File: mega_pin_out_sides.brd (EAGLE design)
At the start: 101.8 x 85 mm, 31 parts, among them T1 2N2222, T2 2N2222, T3 2N2222, T4 2N2222

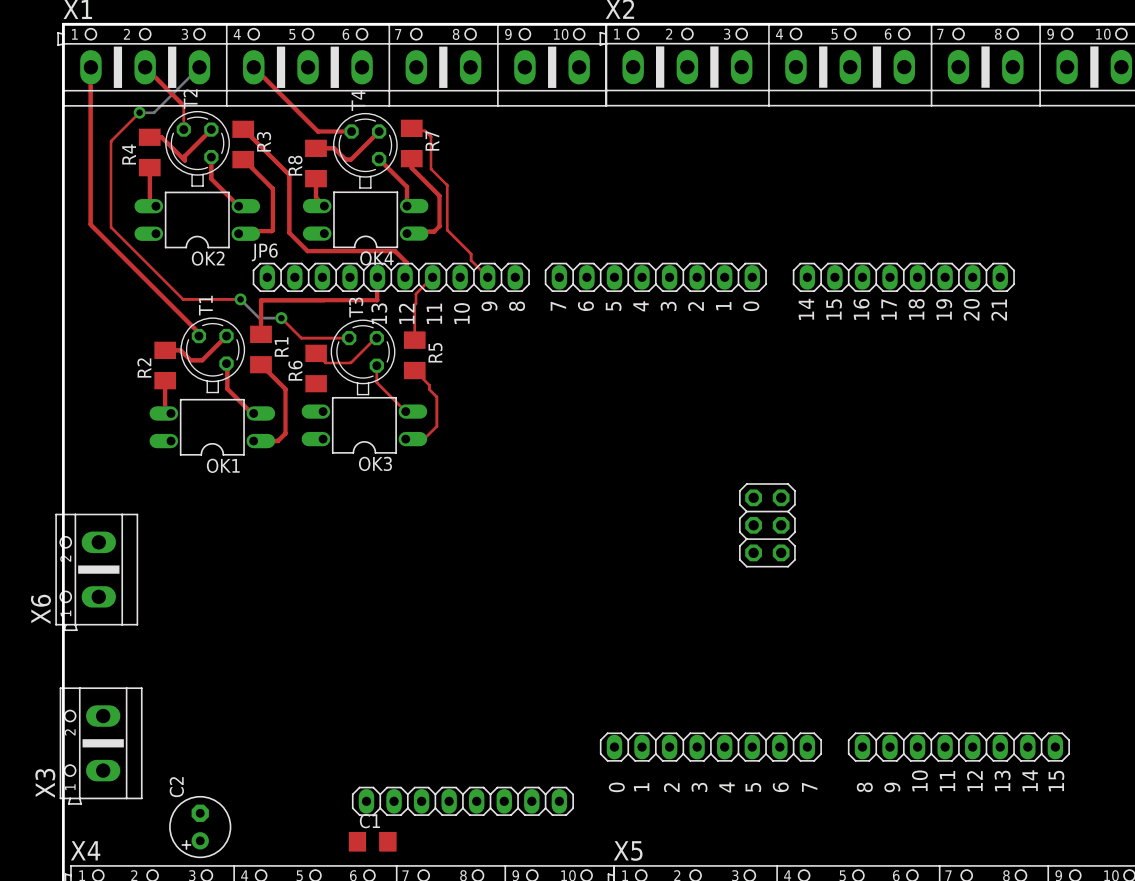
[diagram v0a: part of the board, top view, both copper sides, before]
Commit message: [SIDES] Group same components together
- Grouped same components together and till now this looks a better design solution. to be continued.
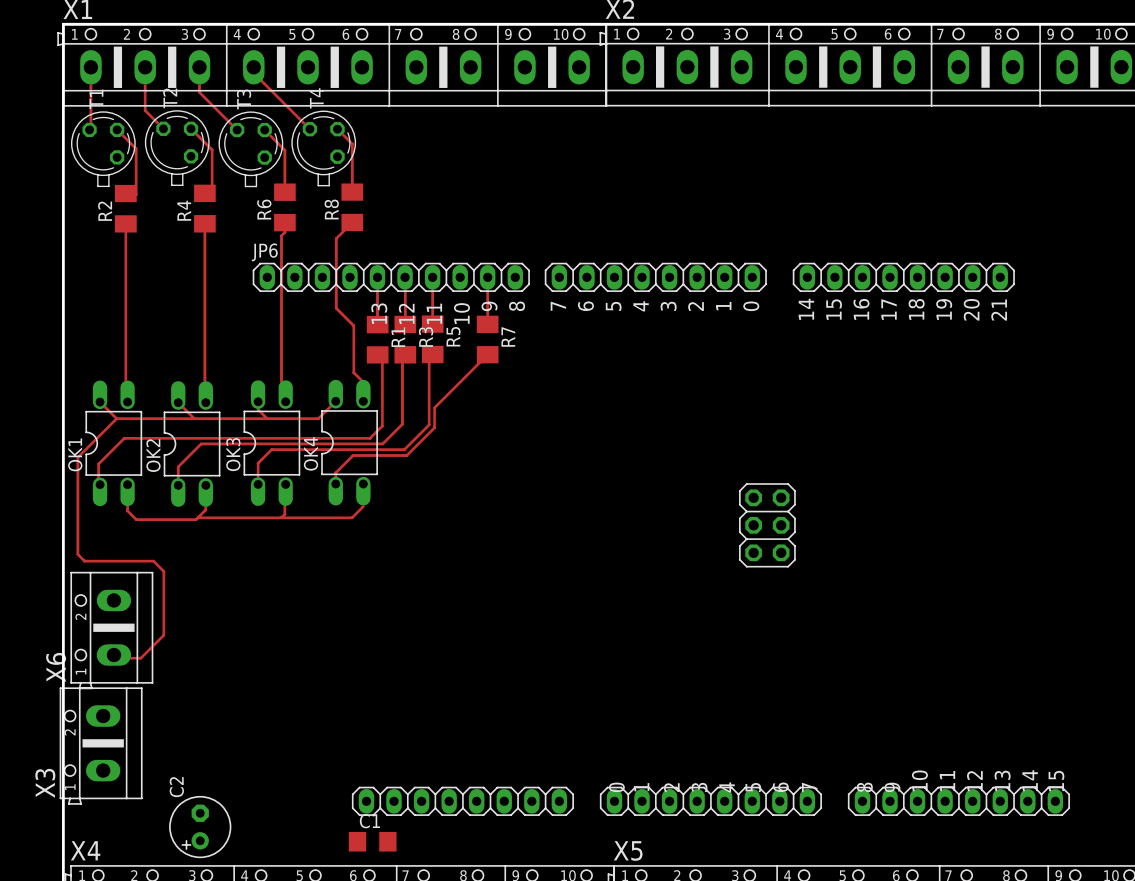
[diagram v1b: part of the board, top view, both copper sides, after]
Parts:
- moved R3 23.4 mm to (31.5, 55.9)
- moved T3 21.8 mm to (17.3, 74.0)
- moved T1 21.5 mm to (3.69, 74.0)
- moved OK2 20.7 mm to (11.9, 46.3), turned to 0 degrees
- moved OK4 20.6 mm to (26.4, 46.4), turned to 0 degrees
- moved R7 19.4 mm to (39.1, 55.9)
- moved R6 15.1 mm to (20.4, 68.1)
- moved R2 14.9 mm to (5.76, 68.0)
- moved R1 10.8 mm to (29.0, 55.9)
- moved OK1 9.20 mm to (4.65, 46.4), turned to 0 degrees
- moved OK3 8.68 mm to (19.2, 46.4), turned to 0 degrees
- moved R4 7.26 mm to (13.0, 68.0)
- moved X6 5.54 mm to (4.66, 29.4)
- moved R8 5.25 mm to (26.6, 68.1)
- moved ADCH 5.00 mm to (82.5, 13.4)
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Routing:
- net VEXT: track 0.00 -> 62.1 mm
- net 11BJT: track 45.1 -> 7.22 mm, vias 3 -> 0
- net N$1: track 10.5 -> 37.9 mm
- net 13BJT: track 28.9 -> 5.89 mm
- net 12: track 24.7 -> 4.35 mm
- net N$5: track 11.1 -> 30.5 mm
- net N$17: track 0.00 -> 16.8 mm
- net N$8: track 9.35 -> 25.8 mm
- net N$20: track 2.84 -> 18.1 mm
- net N$2: track 3.25 -> 16.5 mm
- net 9: track 17.2 -> 4.34 mm
- net N$6: track 3.80 -> 16.5 mm
- net 13: track 16.0 -> 4.36 mm
- net GND: track 22.0 -> 33.6 mm
- net N$19: track 10.6 -> 20.6 mm
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
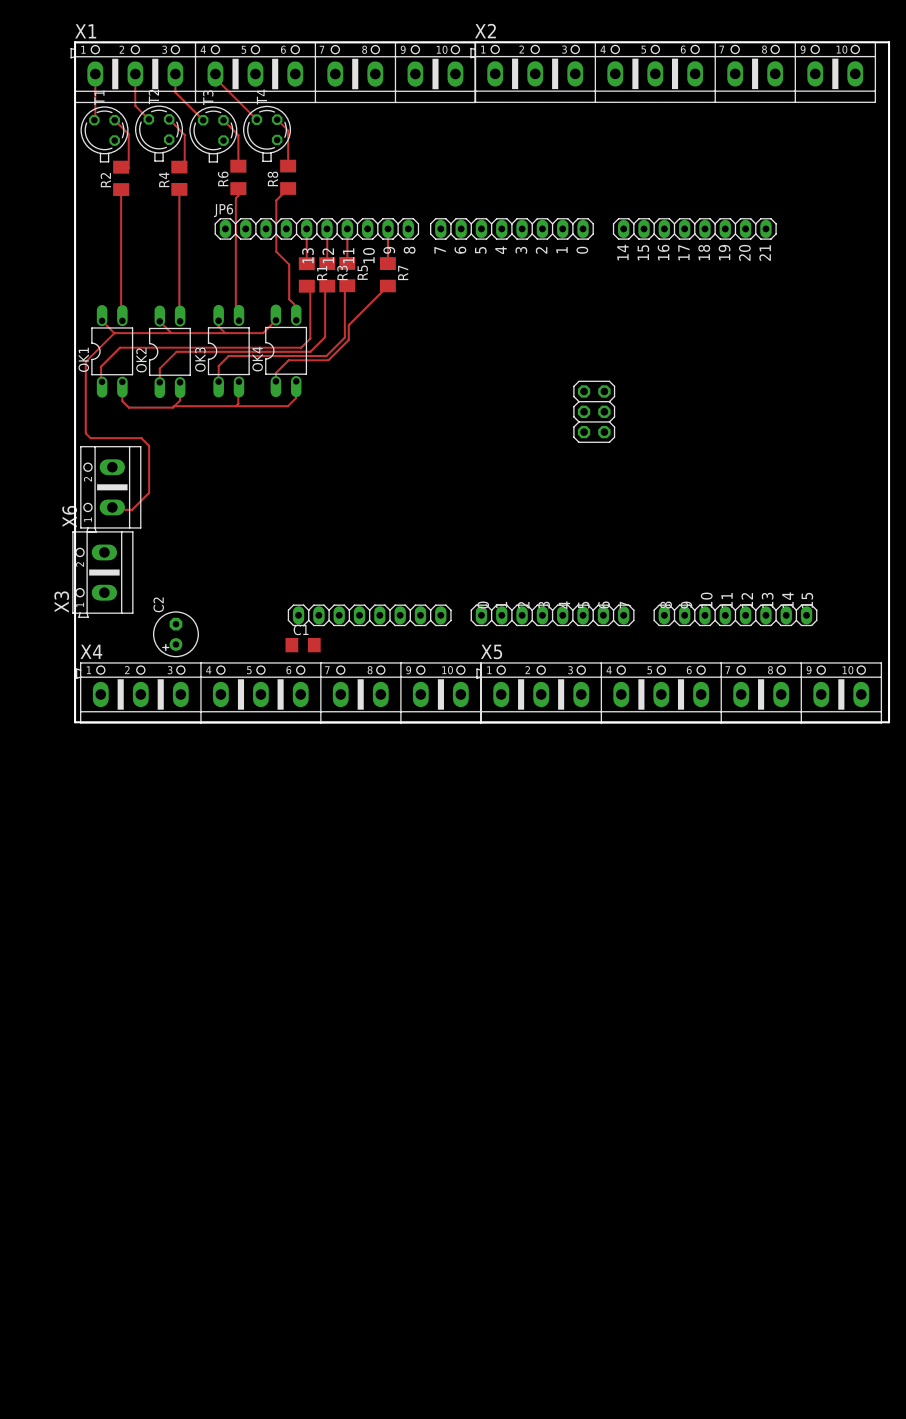
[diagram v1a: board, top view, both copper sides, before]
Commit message: Continue side Schematic design and layout
Almost finished first trail for board layout.
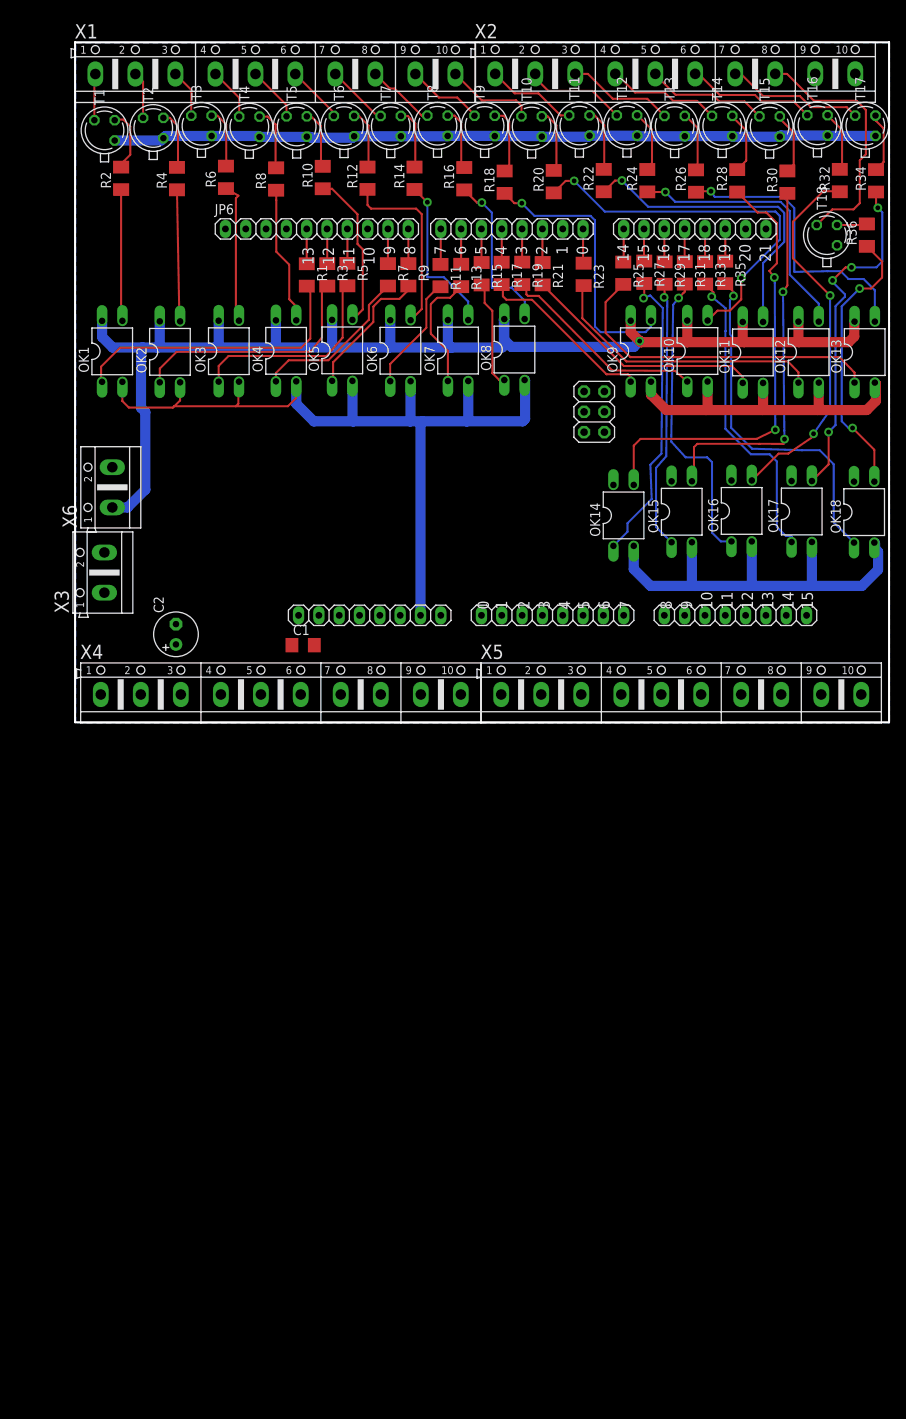
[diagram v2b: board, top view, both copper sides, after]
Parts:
- added OK10, OK11, OK12, OK13, OK14, OK15, OK16, OK17, OK18, OK5, OK6, OK7, OK8, OK9: PC817, optocoupler:DIL04
- added R10, R11, R12, R13, R14, R15, R16, R17, R18, R19, R20, R21, R22, R23, R24, R25, R26, R27, R28, R29, R30, R31, R32, R33, R34, R35, R36, R9: (no value), resistor:M1206
- added T10, T11, T12, T13, T14, T15, T16, T17, T18, T5, T6, T7, T8, T9: 2N2222, transistor:TO18
- moved T4 2.24 mm to (21.8, 74.4)
- moved T3 1.60 mm to (15.8, 74.6)
- moved R6 1.56 mm to (18.9, 68.1)
- moved R8 1.52 mm to (25.1, 67.9)
- moved T2 0.75 mm to (9.77, 74.3)
- moved R4 0.31 mm to (12.7, 68.0)
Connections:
- removed net N$16: X1.5
- new net 0: PWML.1, R23.1
- new net 0BJT: T12.3, X2.2
- new net 14: COMMUNICATION.8, R25.1
- new net 14BJT: T13.3, X2.3
- new net 15: COMMUNICATION.7, R27.1
- new net 15BJT: T14.3, X2.4
- new net 16: COMMUNICATION.6, R29.1
- new net 16BJT: T15.3, X2.5
- new net 17: COMMUNICATION.5, R31.1
- new net 17BJT: T16.3, X2.6
- new net 18: COMMUNICATION.4, R33.1
- new net 18BJT: T17.3, X2.7
- new net 19: COMMUNICATION.3, R35.1
- new net 19BJT: T18.3, X2.8
- new net 2: PWML.3, R21.1
- new net 2BJT: T11.3, X2.1
- new net 3: PWML.4, R19.1
- new net 3BJT: T10.3, X1.10
- new net 4: PWML.5, R17.1
- new net 4BJT: T9.3, X1.9
- new net 5: PWML.6, R15.1
- new net 5BJT: T8.3, X1.8
- new net 6: PWML.7, R13.1
- new net 6BJT: T7.3, X1.7
- new net 7: PWML.8, R11.1
- new net 7BJT: T6.3, X1.6
- new net 8: JP6.10, R9.1
- new net 8BJT: T5.3, X1.5
- new net N$14: OK5.1, R9.2
- new net N$15: OK5.3, R10.1
- new net N$22: R10.2, T5.2
- new net N$23: OK6.1, R11.2
- new net N$24: OK6.3, R12.1
- new net N$25: R12.2, T6.2
- new net N$26: OK7.1, R13.2
- new net N$27: OK7.3, R14.1
- new net N$28: R14.2, T7.2
- new net N$29: OK8.1, R15.2
- new net N$30: OK8.3, R16.1
- new net N$31: R16.2, T8.2
- new net N$32: OK9.1, R17.2
- new net N$33: OK9.3, R18.1
- new net N$34: R18.2, T9.2
- new net N$35: OK10.1, R19.2
- new net N$36: OK10.3, R20.1
- new net N$37: R20.2, T10.2
- new net N$38: OK11.1, R21.2
- new net N$39: OK11.3, R22.1
- new net N$40: R22.2, T11.2
- new net N$41: OK16.1, R31.2
- new net N$42: OK16.3, R32.1
- new net N$43: R32.2, T16.2
- new net N$44: OK12.1, R23.2
- new net N$45: OK12.3, R24.1
- new net N$46: R24.2, T12.2
- new net N$47: OK13.1, R25.2
- new net N$48: OK13.3, R26.1
- new net N$49: R26.2, T13.2
- new net N$50: OK14.1, R27.2
- new net N$51: OK14.3, R28.1
- new net N$52: R28.2, T14.2
- new net N$53: OK15.1, R29.2
- new net N$54: OK15.3, R30.1
- new net N$55: R30.2, T15.2
- new net N$56: OK18.1, R35.2
- new net N$57: OK18.3, R36.1
- new net N$58: R36.2, T18.2
- new net N$59: OK17.1, R33.2
- new net N$60: OK17.3, R34.1
- new net N$61: R34.2, T17.2
- new net N$77: COMMUNICATION.2
- new net N$78: COMMUNICATION.1
- new net N$92: X2.9
- new net N$93: X2.10
- net GND: now also OK10.2, OK11.2, OK12.2, OK13.2, OK14.2, OK15.2, OK16.2, OK17.2, OK18.2, OK5.2, OK6.2, OK7.2, OK8.2, OK9.2, T10.1, T11.1, T12.1, T13.1, T14.1, T15.1, T16.1, T17.1, T18.1, T5.1, T6.1, T7.1, T8.1, T9.1
- net VEXT: now also OK10.4, OK11.4, OK12.4, OK13.4, OK14.4, OK15.4, OK16.4, OK17.4, OK18.4, OK5.4, OK6.4, OK7.4, OK8.4, OK9.4
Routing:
- net GND: track 33.6 -> 305.7 mm
- net VEXT: track 62.1 -> 161.2 mm, vias 0 -> 1
- net N$51: track 0.00 -> 56.2 mm, vias 0 -> 2
- net N$36: track 0.00 -> 48.4 mm, vias 0 -> 2
- net N$54: track 0.00 -> 47.2 mm, vias 0 -> 2
- net N$42: track 0.00 -> 46.6 mm, vias 0 -> 2
- net N$56: track 0.00 -> 44.3 mm, vias 0 -> 1
- net N$60: track 0.00 -> 43.6 mm, vias 0 -> 4
- net N$47: track 0.00 -> 41.4 mm
- net N$39: track 0.00 -> 39.6 mm, vias 0 -> 1
- net N$59: track 0.00 -> 38.7 mm, vias 0 -> 1
- net N$41: track 0.00 -> 38.2 mm, vias 0 -> 1
- net N$50: track 0.00 -> 37.3 mm, vias 0 -> 1
- net N$48: track 0.00 -> 36.3 mm, vias 0 -> 1
- net N$44: track 0.00 -> 35.2 mm
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- added copper zone on layer 16, net GND

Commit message: [SIDES] New design proposal
- In this commit the layout was completely changed. Opto are grouped in the center while BJT was beside the terminal blocks.

TODO: complete the Analogue side.
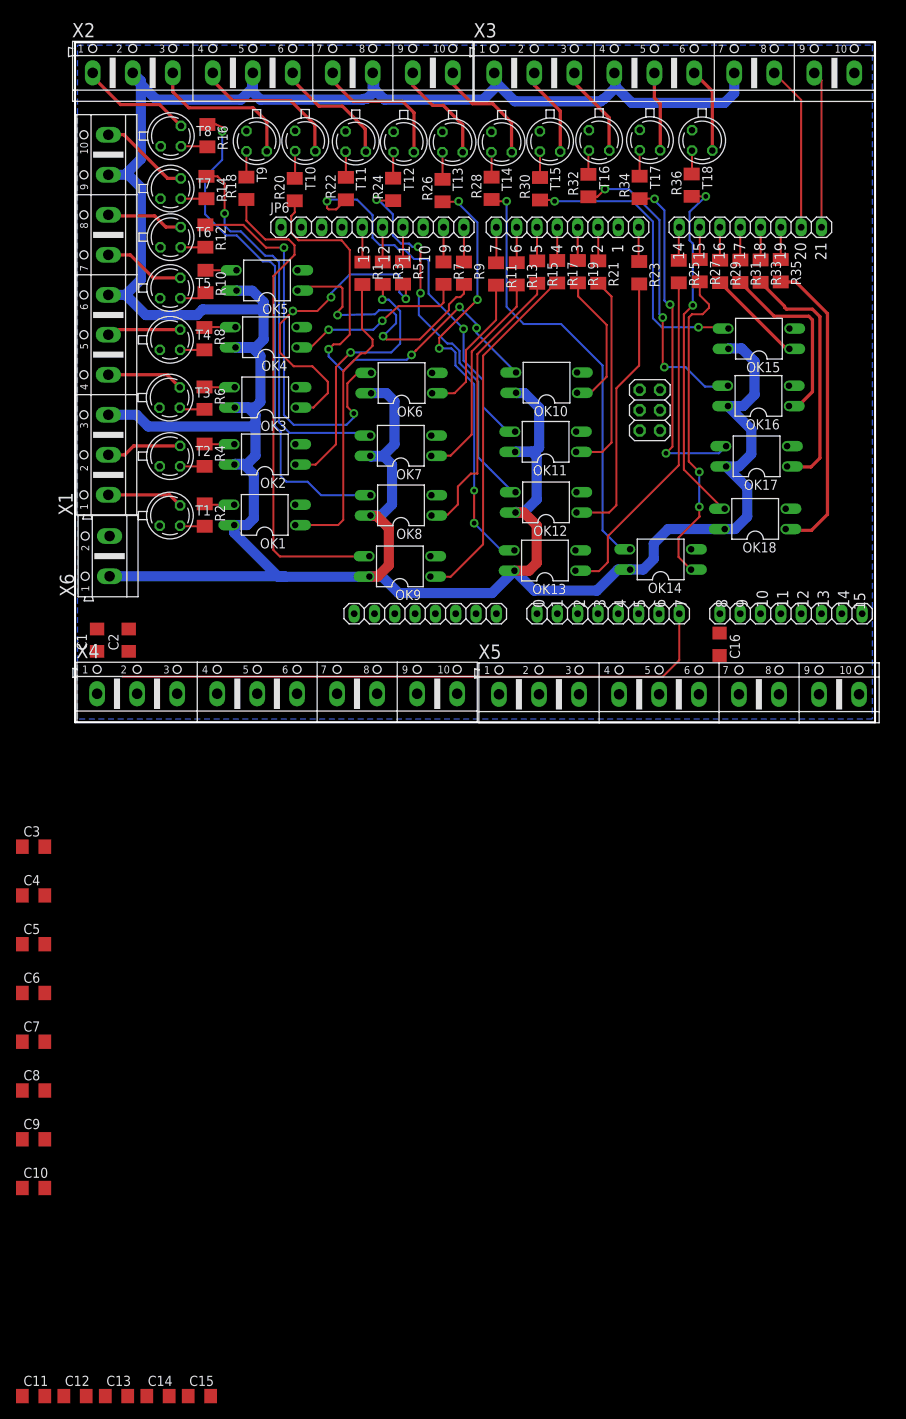
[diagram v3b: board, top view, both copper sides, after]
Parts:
- added C10, C11, C12, C13, C14, C15, C16, C3, C4, C5, C6, C7, C8, C9: (no value), resistor:C1206
- C2: device rcl:E2,5-6 -> resistor:C1206
- X3: device con-ptr500:AK500/2 -> con-ptr500:AK500/10
- moved X3 94.7 mm to (74.9, 81.2), turned to 0 degrees
- moved X2 50.3 mm to (24.7, 81.2)
- moved T1 48.8 mm to (11.9, 25.8), turned to 0 degrees
- moved OK13 47.7 mm to (58.7, 20.2), turned to 90 degrees
- moved R2 43.4 mm to (16.2, 25.9), turned to 270 degrees
- moved T2 41.1 mm to (11.9, 33.3), turned to 0 degrees
- moved OK9 40.4 mm to (40.6, 19.5), turned to 90 degrees
- moved OK12 37.8 mm to (58.9, 27.5), turned to 90 degrees
- moved X1 36.6 mm to (4.16, 50.9), turned to 90 degrees
- moved R4 34.7 mm to (16.2, 33.4), turned to 270 degrees
- moved T3 34.2 mm to (11.8, 40.6), turned to 0 degrees
- moved T8 33.4 mm to (12.0, 73.3), turned to 0 degrees
- moved R16 32.6 mm to (16.5, 73.3), turned to 270 degrees
- moved R20 32.4 mm to (27.5, 66.6)
- moved R18 32.3 mm to (21.4, 66.7)
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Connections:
- net N$11 renamed RST
- removed net N$10: POWER.4
- removed net N$3: POWER.8
- removed net N$77: COMMUNICATION.2
- removed net N$78: COMMUNICATION.1
- removed net N$9: POWER.5
- removed net N$92: X2.9
- removed net N$93: X2.10
- new net 3V3: POWER.4, X4.1
- new net 5V: POWER.5, X4.2
- new net A0: ADCL.8, X4.5
- new net A1: ADCL.7, X4.6
- new net A10: ADCH.6, C11.1, X5.5
- new net A11: ADCH.5, C12.1, X5.6
- new net A12: ADCH.4, C13.1, X5.7
- new net A13: ADCH.3, C14.1, X5.8
- new net A14: ADCH.2, C15.1, X5.9
- new net A15: ADCH.1, C16.1, X5.10
- new net A2: ADCL.6, X4.7
- new net A3: ADCL.5, X4.8
- new net A4: ADCL.4, X4.9
- new net A5: ADCL.3, X4.10
- new net A6: ADCL.2, X5.1
- new net A7: ADCL.1, X5.2
- new net A8: ADCH.8, X5.3
- new net A9: ADCH.7, X5.4
- new net SCL: COMMUNICATION.1, X3.9
- new net SDA: COMMUNICATION.2, X3.8
- new net VIN: POWER.8, X4.4
- net 0BJT: now also X2.7; no longer X2.2
- net 11BJT: now also X1.4; no longer X1.3
- net 14BJT: now also X2.9; no longer X2.3
- net 15BJT: now also X2.10; no longer X2.4
- net 16BJT: now also X3.2; no longer X2.5
- net 17BJT: now also X3.3; no longer X2.6
- net 18BJT: now also X3.5; no longer X2.7
- net 19BJT: now also X3.6; no longer X2.8
- net 2BJT: now also X2.6; no longer X2.1
- net 3BJT: now also X2.4; no longer X1.10
- net 4BJT: now also X2.3; no longer X1.9
- net 5BJT: now also X2.1; no longer X1.8
- net 6BJT: now also X1.10; no longer X1.7
- net 7BJT: now also X1.8; no longer X1.6
- net 8BJT: now also X1.7; no longer X1.5
- net 9BJT: now also X1.5; no longer X1.4
- net GND: now also C1.2, C10.2, C11.2, C12.2, C13.2, C14.2, C15.2, C16.2, C2.2, C3.2, C4.2, C5.2, C6.2, C7.2, C8.2, C9.2, X4.3
- net VEXT: now also X1.3, X1.6, X1.9, X2.2, X2.5, X2.8, X3.1, X3.4, X3.7
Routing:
- net GND: track 305.7 -> 0.00 mm
- net VEXT: track 161.2 -> 415.0 mm, vias 1 -> 0
- net A0: track 0.00 -> 76.3 mm
- net N$30: track 21.1 -> 63.8 mm
- net N$27: track 20.3 -> 48.7 mm
- net N$33: track 34.3 -> 61.5 mm, vias 1 -> 0
- net N$24: track 23.0 -> 49.7 mm, vias 0 -> 2
- net N$32: track 22.3 -> 45.0 mm
- net N$29: track 13.4 -> 36.1 mm
- net 19BJT: track 31.7 -> 10.6 mm
- net N$53: track 33.7 -> 12.9 mm, vias 1 -> 0
- net SDA: track 0.00 -> 20.7 mm
- net SCL: track 0.00 -> 19.7 mm
- net N$48: track 36.3 -> 54.4 mm, vias 1 -> 5
- net N$14: track 17.2 -> 34.8 mm, vias 0 -> 2
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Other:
- board size 101.8 x 85 mm -> 100 x 85 mm
